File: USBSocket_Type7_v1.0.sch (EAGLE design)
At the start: 8 parts, among them X1 USBPCB

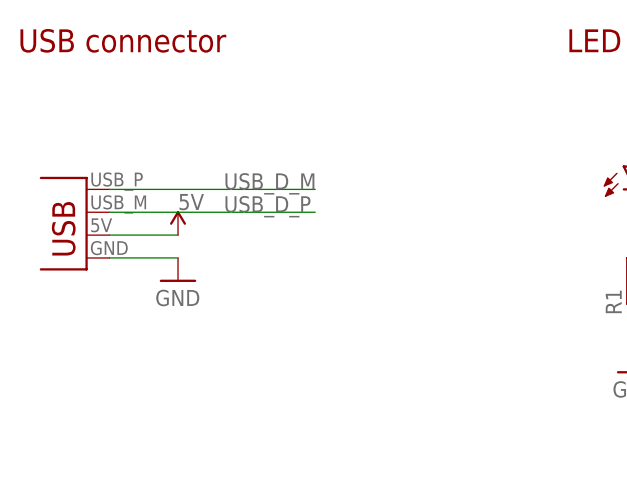
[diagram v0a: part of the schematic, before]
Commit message: Fixed schematic and routing for t7 board.
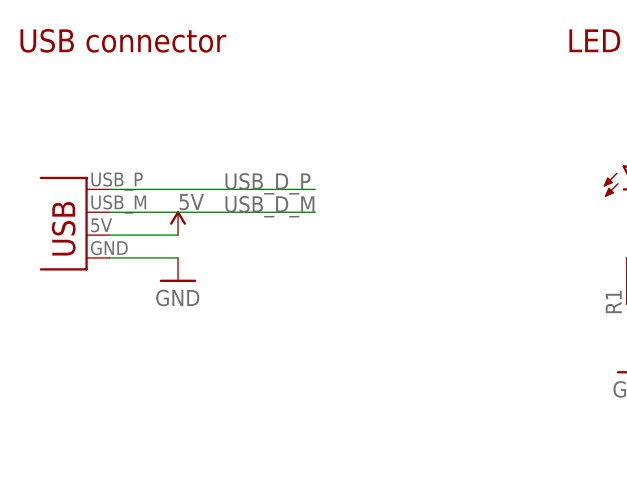
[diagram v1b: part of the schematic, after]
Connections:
- net USB_D_M: now also X1.D-; no longer X1.D+
- net USB_D_P: now also X1.D+; no longer X1.D-
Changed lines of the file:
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@@
 <net name="USB_D_M" class="1">
-<segment>
-<wire x1="73.66" y1="101.6" x2="50.8" y2="101.6" width="0.1524" layer="91"/>
-<label x="63.5" y="101.6" size="1.778" layer="95"/>
-<pinref part="X1" gate="G$1" pin="D+"/>
-</segment>
 <segment>
 <pinref part="J1" gate="G$1" pin="2"/>
@@
 <label x="200.66" y="101.6" size="1.778" layer="95"/>
 </segment>
+<segment>
+<pinref part="X1" gate="G$1" pin="D-"/>
+<wire x1="50.8" y1="99.06" x2="73.66" y2="99.06" width="0.1524" layer="91"/>
+<label x="63.5" y="99.06" size="1.778" layer="95"/>
+</segment>
 </net>
 <net name="USB_D_P" class="1">
-<segment>
-<wire x1="50.8" y1="99.06" x2="73.66" y2="99.06" width="0.1524" layer="91"/>
-<label x="63.5" y="99.06" size="1.778" layer="95"/>
-<pinref part="X1" gate="G$1" pin="D-"/>
-</segment>
 <segment>
 <pinref part="J1" gate="G$1" pin="3"/>
@@
 <label x="200.66" y="99.06" size="1.778" layer="95"/>
 </segment>
+<segment>
+<pinref part="X1" gate="G$1" pin="D+"/>
+<wire x1="50.8" y1="101.6" x2="73.66" y2="101.6" width="0.1524" layer="91"/>
+<label x="63.5" y="101.6" size="1.778" layer="95"/>
+</segment>
 </net>
